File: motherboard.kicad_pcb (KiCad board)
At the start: 2 copper layers, 90.2 x 95.9 mm, 109 parts, among them P1 CONN_02X08, U1 STM32F411-LQFP64, U10 74LS125, U11 74LS125, U12 74LS125, U13 74LS125, U14 PCA9517A, U15 PCA9517A, U16 74LS125, U17 74LS125, U2 STM32F411-LQFP64, U3 AP7313, U4 74LS00, U5 74LS125, U6 FM25V20A-G, U7 FM25V20A-G, U8 FM25V20A-G, U9 FM25V20A-G, Y1 32k, Y2 8M(16pF), Y3 32k, Y4 8M(16pF)

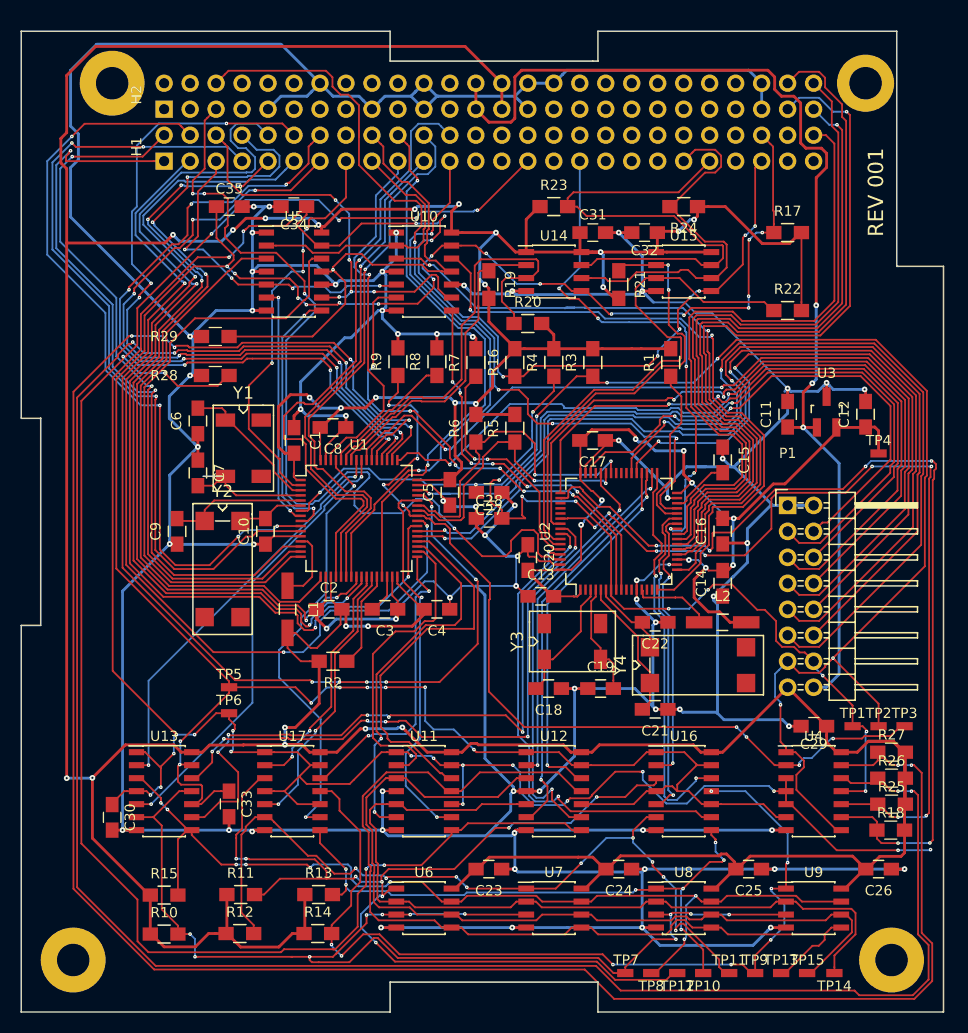
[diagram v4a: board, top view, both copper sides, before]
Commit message: Fixed wireplacement, moved values to facilitate eaiser assembly, Added text and logo
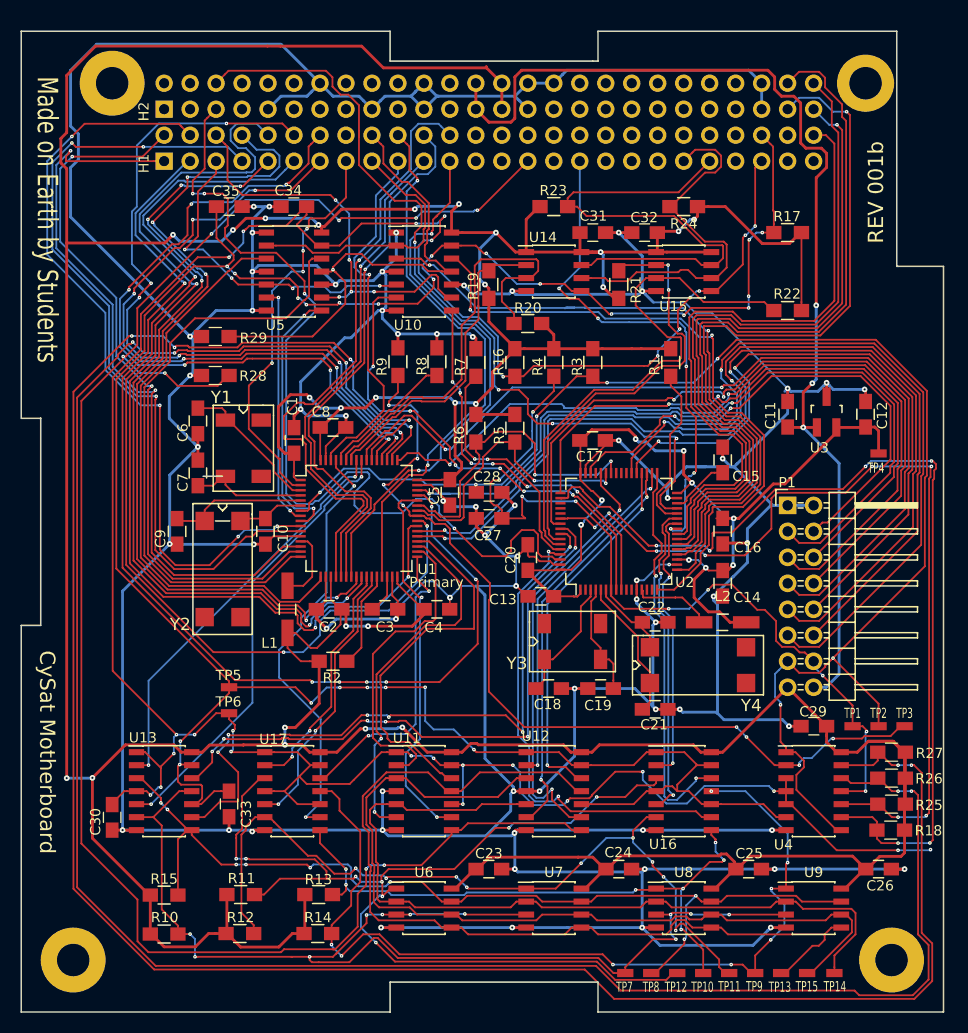
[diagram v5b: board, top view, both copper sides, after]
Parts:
- added LOGO: , AeroE294:LOGO, B.Cu at (191.5, 119.9)
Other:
- board text added: "CySat Motherboard"
- board text added: "Made on Earth by Students"
- board text added: "Primary"
- board text added: "REV 001b"
- board text removed: "REV 001"
